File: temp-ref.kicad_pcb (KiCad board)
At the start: 4 copper layers, 172.5 x 76.5 mm, 42 parts, among them IC1 INA211AIDCKT, IC2 INA211AIDCKT, J1 Conn_01x05_Male, J2 USB_C_Receptacle_USB2.0, Q1 Q_NMOS_GDS, Q3 Q_NMOS_GDS, SW1 SW_SPST, SW2 SW_SPST, SW3 SW_SPST, SW4 SW_SPST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

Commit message: layout attempt 1
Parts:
- added Q2: MMBT3904, Package_TO_SOT_SMD:SOT-23, F.Cu at (151.8, 48.4)
- added R3: 10k, Resistor_SMD:R_0603_1608Metric, F.Cu at (151.6, 52.6)
- added R5: 10k, Resistor_SMD:R_0603_1608Metric, F.Cu at (151.6, 51.0)
- added R9: 33, Resistor_SMD:R_0603_1608Metric, F.Cu at (148.6, 47.4)
- J2: footprint Connector_USB:USB_C_Receptacle_JAE_DX07S024WJ3R400 -> Connector_USB:USB_C_Receptacle_Amphenol_12401610E4-2A
- SW1, SW2, SW3, SW4: footprint Button_Switch_SMD:SW_Push_1P1T_NO_CK_KSC7xxJ -> temp-ref:5.2mm_Tact_reverse_mount
- U6: value adafruit-tft-120x135-4383 -> spi-tft-1.14-240x135; footprint temp-ref:adafruit-tft-4383 -> temp-ref:TFT-1.14-240-135; moved to B.Cu
- moved U5 84.9 mm to (31.8, 61.6)
- moved U1 55.6 mm to (94.2, 60.0)
- moved U6 16.7 mm to (135.5, 32.7), turned to 90 degrees
- moved IC1 12.3 mm to (148.0, 85.3), turned to 270 degrees
- moved IC2 11.5 mm to (138.0, 85.3), turned to 270 degrees
- moved C8 10.8 mm to (148.1, 87.8), turned to 180 degrees
- moved J2 10.1 mm to (143.0, 95.5), turned to 0 degrees
- moved C5 9.80 mm to (137.9, 87.8), turned to 180 degrees
- moved U7 6.86 mm to (145.1, 86.0), turned to 180 degrees
- moved U10 6.22 mm to (140.9, 86.0), turned to 180 degrees
- turned SW1 to 90 degrees
- turned SW2 to 90 degrees
- turned SW3 to 90 degrees
- turned SW4 to 90 degrees
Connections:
- U4 pad 10: Net-(U4-Pad10) -> WIFI_G2
- U4 pad 15: Net-(U4-Pad15) -> WIFI_TX
- U4 pad 16: Net-(U4-Pad16) -> WIFI_RX
- U4 pad 21: Net-(U4-Pad21) -> WIFI_G0
- U4 pad 9: Net-(U4-Pad9) -> WIFI_RST
- U6 pad 1: +3V3 -> (no net)
- U6 pad 10: DISP_SDCS -> +3V3
- U6 pad 11: DISP_BACKLIGHT -> Net-(R9-Pad2)
- U6 pad 2: Net-(U6-Pad2) -> (no net)
- U6 pad 3: GND -> DISP_MOSI
- U6 pad 5: DISP_MISO -> DISP_DC
- U6 pad 6: DISP_MOSI -> DISP_RST
- U6 pad 8: DISP_RST -> GND
- U6 pad 9: DISP_DC -> (no net)
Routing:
- net SCL: track 13.4 -> 183.3 mm, vias 0 -> 5
- net +3V3: track 39.4 -> 183.7 mm, vias 13 -> 15
- net SDA: track 12.9 -> 148.0 mm, vias 0 -> 3
- net KEYB: track 1.24 -> 41.0 mm, vias 1 -> 0
- net VBUS: track 35.5 -> 72.0 mm, vias 14 -> 28
- net KEYA: track 1.04 -> 34.7 mm, vias 1 -> 0
- net DISP_SCK: track 0.00 -> 31.9 mm, vias 0 -> 3
- net DISP_MOSI: track 0.00 -> 31.6 mm, vias 0 -> 3
- net DISP_BACKLIGHT: track 0.00 -> 28.1 mm, vias 0 -> 2
- net KEYC: track 1.14 -> 26.9 mm, vias 1 -> 0
- net KEYD: track 1.12 -> 24.4 mm, vias 1 -> 0
- net B_SENSE: track 39.2 -> 16.0 mm, vias 4 -> 3
- net DISP_CS: track 0.00 -> 22.6 mm, vias 0 -> 1
- net DISP_RST: track 0.00 -> 22.6 mm, vias 0 -> 1
- net DISP_DC: track 0.00 -> 22.3 mm, vias 0 -> 1
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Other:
- outline, holes or cut-outs redrawn
- rule pad_to_mask_clearance: 0.002 -> 0

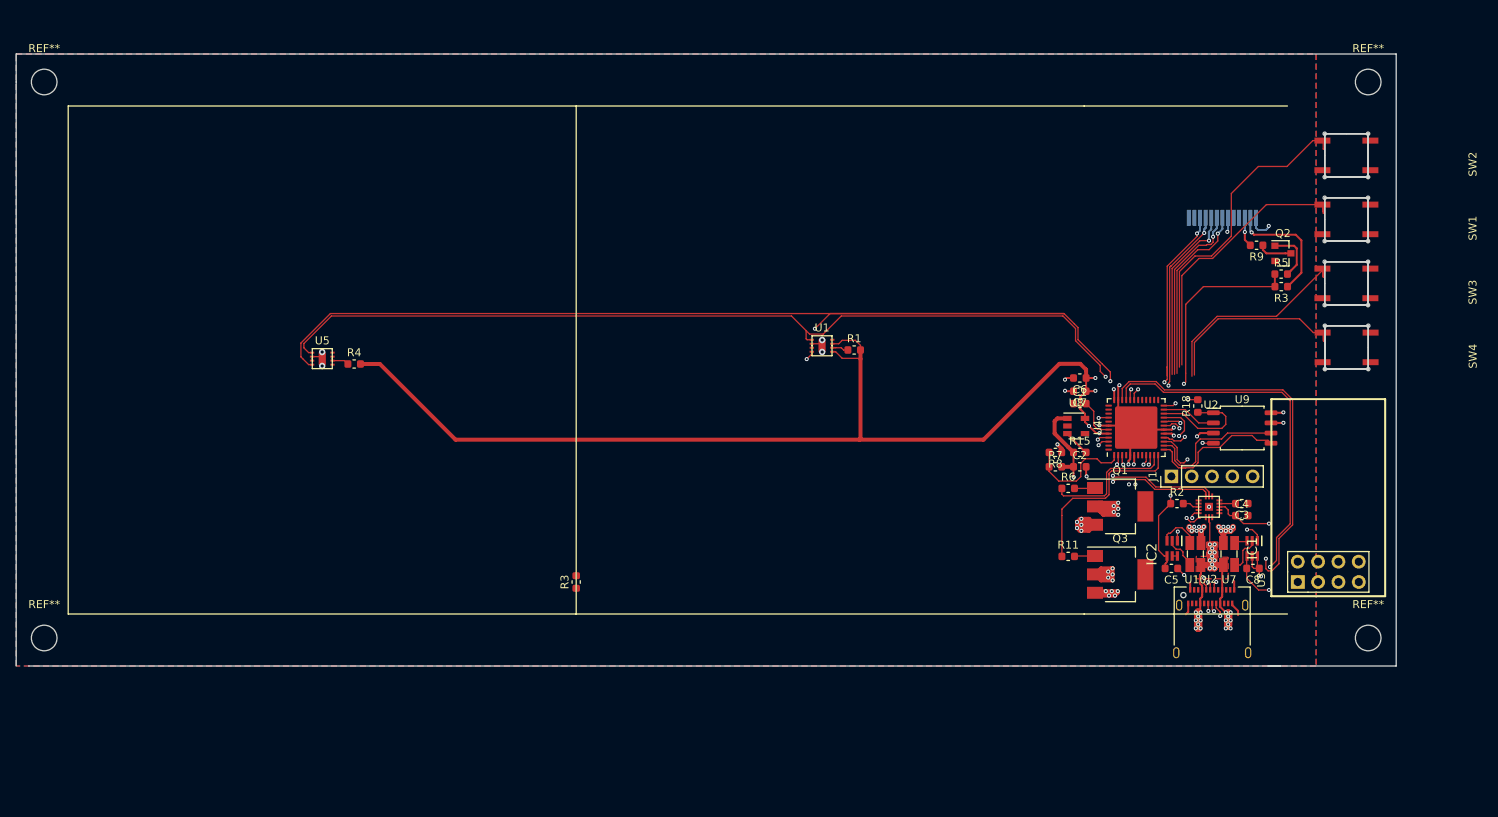
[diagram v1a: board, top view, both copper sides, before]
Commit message: REworked electronics into smaller board. Heating elements will be seperate.
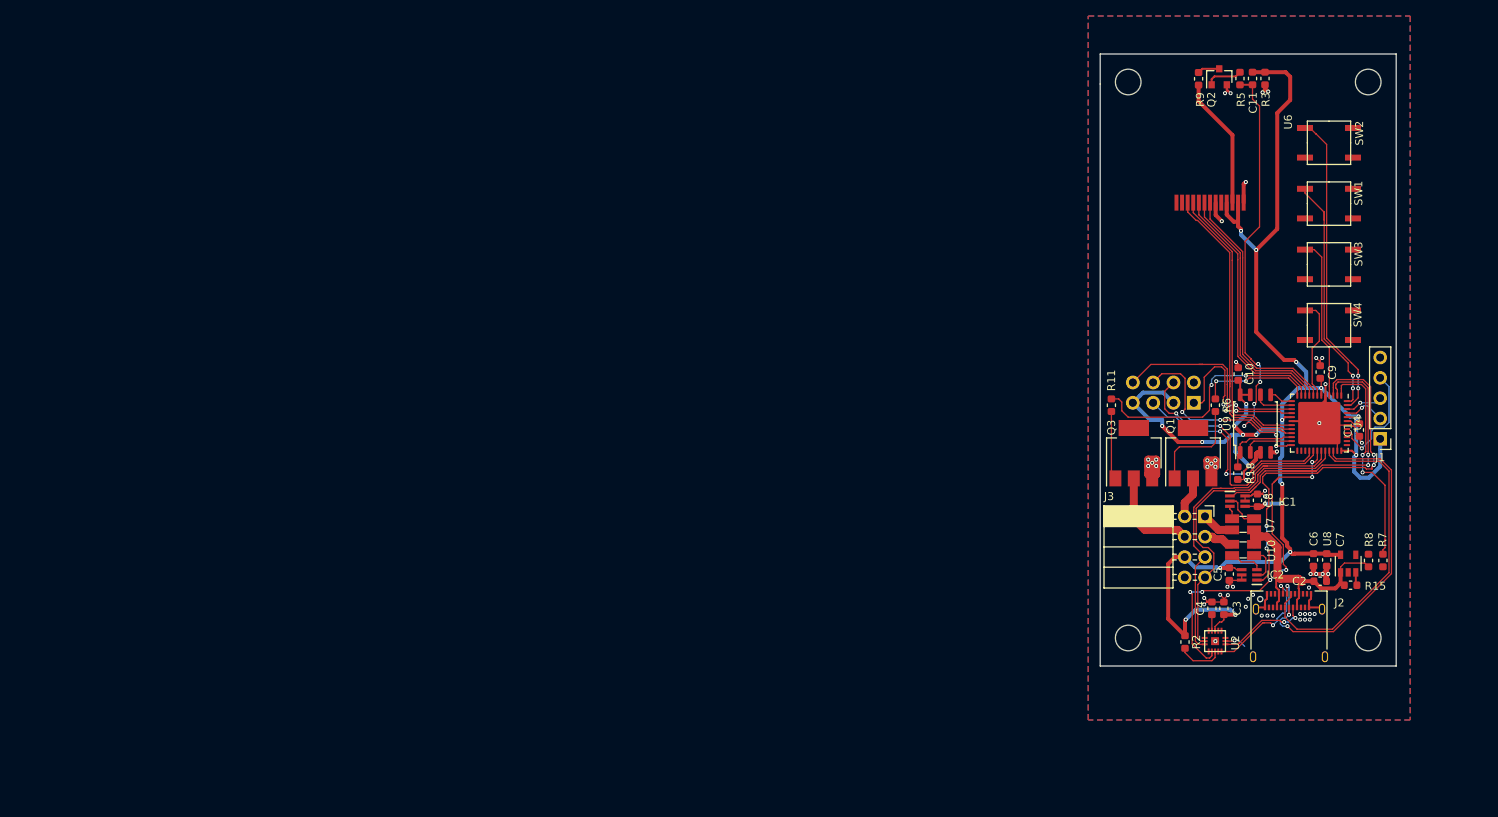
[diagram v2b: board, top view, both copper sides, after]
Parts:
- removed R1, R4: 1k, Resistor_SMD:R_0603_1608Metric
- removed the R3 at (63.5, 89.5)
- removed the REF** at (-3.00, 96.5)
- removed the REF** at (-3.00, 27.0)
- removed U1, U5: STS-30-DIS, temp-ref:sts
- added C10: 1uF, Capacitor_SMD:C_0603_1608Metric, F.Cu at (146.2, 63.5)
- added C11: 1uF, Capacitor_SMD:C_0603_1608Metric, F.Cu at (149.6, 26.6)
- added C9: 1uF, Capacitor_SMD:C_0603_1608Metric, F.Cu at (156.5, 63.2)
- added J3: Conn_02x04_Counter_Clockwise, Connector_PinSocket_2.54mm:PinSocket_2x04_P2.54mm_Horizontal, F.Cu at (142.1, 81.3)
- added REF**: MountingHole_3.2mm_M3, MountingHole:MountingHole_3.2mm_M3, F.Cu at (132.5, 96.5)
- added REF**: MountingHole_3.2mm_M3, MountingHole:MountingHole_3.2mm_M3, F.Cu at (132.5, 27.0)
- U3: moved to B.Cu
- U6: moved to F.Cu
- moved R8 43.1 mm to (164.3, 86.8), turned to 90 degrees
- moved R7 40.9 mm to (162.5, 86.8), turned to 270 degrees
- moved U8 38.1 mm to (160.0, 87.2), turned to 90 degrees
- moved R15 37.7 mm to (160.3, 89.9)
- moved C7 37.4 mm to (157.3, 86.7), turned to 270 degrees
- moved C6 37.0 mm to (155.7, 86.7), turned to 270 degrees
- moved C1 35.1 mm to (161.4, 70.5), turned to 90 degrees
- moved C2 33.3 mm to (156.5, 89.4)
- moved J1 26.5 mm to (164.0, 71.6), turned to 180 degrees
- moved R3 26.3 mm to (148.0, 26.6), turned to 270 degrees
- moved U3 25.9 mm to (140.7, 67.1)
- moved R5 25.0 mm to (146.5, 26.6), turned to 90 degrees
- moved Q2 23.5 mm to (143.9, 26.4), turned to 90 degrees
- moved U4 22.9 mm to (156.4, 69.6), turned to 270 degrees
- moved R9 22.0 mm to (141.3, 26.6), turned to 270 degrees
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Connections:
- Q1 pad 2: ZONEA -> ZONEA-
- Q3 pad 2: ZONEB -> ZONEB-
- U10 pad 3: ZONEB -> ZONEB+
- U4 pad 10: WIFI_G2 -> DISP_DC
- U4 pad 11: HEATER0 -> HEATER1
- U4 pad 12: HEATER1 -> HEATER0
- U4 pad 2: B_SENSE -> A_SENSE
- U4 pad 28: Net-(U4-Pad28) -> WIFI_RST
- U4 pad 29: Net-(U4-Pad29) -> WIFI_G2
- U4 pad 3: A_SENSE -> B_SENSE
- U4 pad 30: Net-(U4-Pad30) -> PD_ALERT
- U4 pad 4: Net-(U4-Pad4) -> KEYC
- U4 pad 47: Net-(U4-Pad47) -> KEYB
- U4 pad 48: Net-(U4-Pad48) -> KEYA
- U4 pad 7: Net-(U4-Pad7) -> KEYD
- U4 pad 8: Net-(U4-Pad8) -> DISP_CS
- U4 pad 9: WIFI_RST -> DISP_RST
- U7 pad 4: ZONEA -> ZONEA+
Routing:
- net ZONEB: track 4060.3 -> 0.00 mm, vias 12 -> 0
- net ZONEA: track 3705.1 -> 0.00 mm, vias 12 -> 0
- net SCL: track 183.3 -> 39.6 mm, vias 5 -> 0
- net SDA: track 148.0 -> 39.7 mm, vias 3 -> 0
- net PD_ALERT: track 0.00 -> 44.9 mm, vias 0 -> 6
- net VBUS: track 72.0 -> 36.3 mm, vias 28 -> 1
- net +3V3: track 183.7 -> 214.9 mm, vias 15 -> 22
- net B_SENSE: track 16.0 -> 46.1 mm, vias 3 -> 4
- net DISP_BACKLIGHT: track 28.1 -> 55.3 mm, vias 2 -> 6
- net GND: track 72.4 -> 93.6 mm, vias 28 -> 48
- net A_SENSE: track 25.7 -> 44.9 mm, vias 3 -> 2
- net D+: track 64.5 -> 46.3 mm
- net D-: track 58.1 -> 41.3 mm, vias 3 -> 0
- net WIFI_TX: track 36.6 -> 20.5 mm, vias 1 -> 2
- net FLMOSI: track 18.6 -> 2.96 mm
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- removed copper zone on In2.Cu, net +3V3
- removed copper zone on In1.Cu, net GND
- removed copper zone on F.Cu, net VBUS
- removed copper zone on In2.Cu, net VBUS
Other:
- board size 172.5 x 76.5 mm -> 37 x 76.5 mm
- copper layers 4 -> 2

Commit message: Update temp-ref.kicad_pcb
removed errant via
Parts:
- added D1: SK6812, LED_SMD:LED_SK6812_PLCC4_5.0x5.0mm_P3.2mm, F.Cu at (157.6, 80.2)
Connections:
- U4 pad 27: Net-(U4-Pad27) -> neopix
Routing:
- net neopix: track 0.00 -> 13.8 mm, vias 0 -> 2
- net VBUS: track 36.3 -> 45.2 mm
- net +3V3: track 214.9 -> 218.7 mm
- net GND: track 93.6 -> 96.4 mm, vias 48 -> 49
- net (no net): vias 2 -> 1

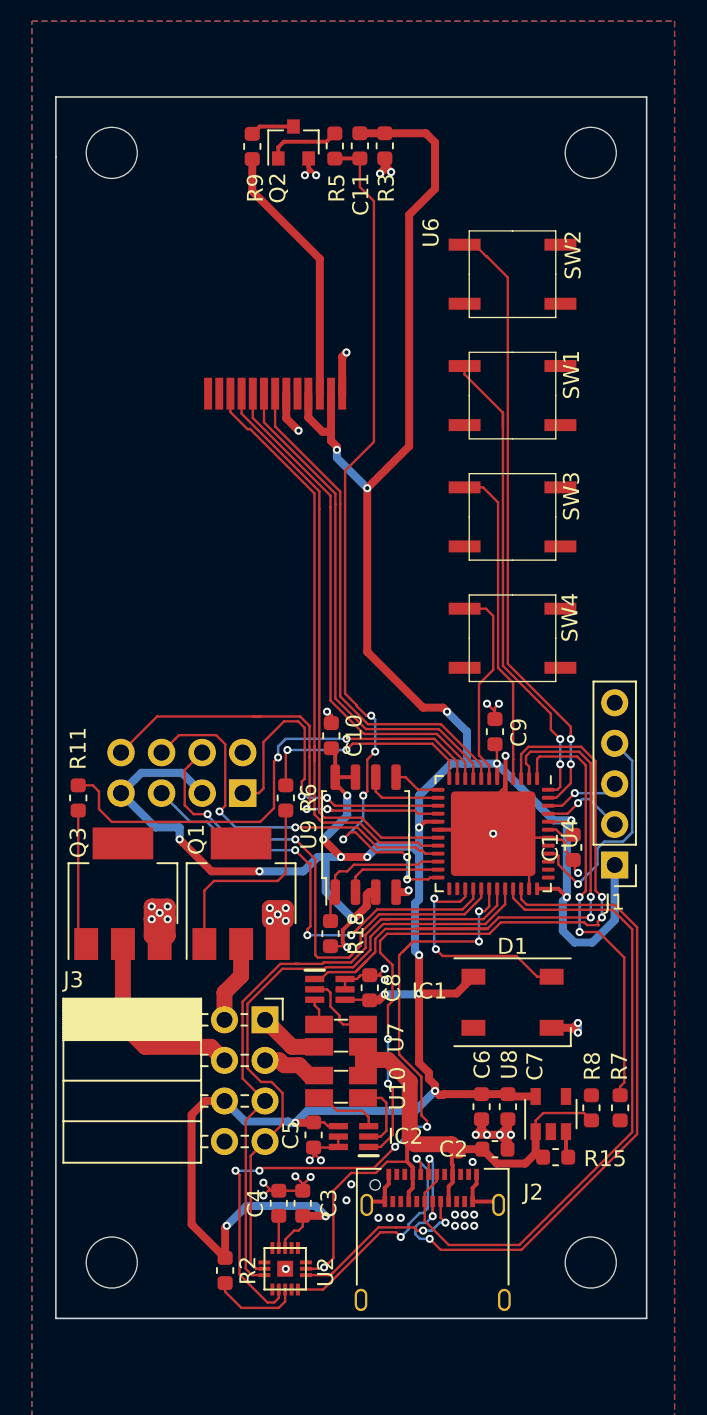
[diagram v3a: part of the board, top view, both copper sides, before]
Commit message: 3d models added, Added dallas pins, added nepixels, moved some elements around.
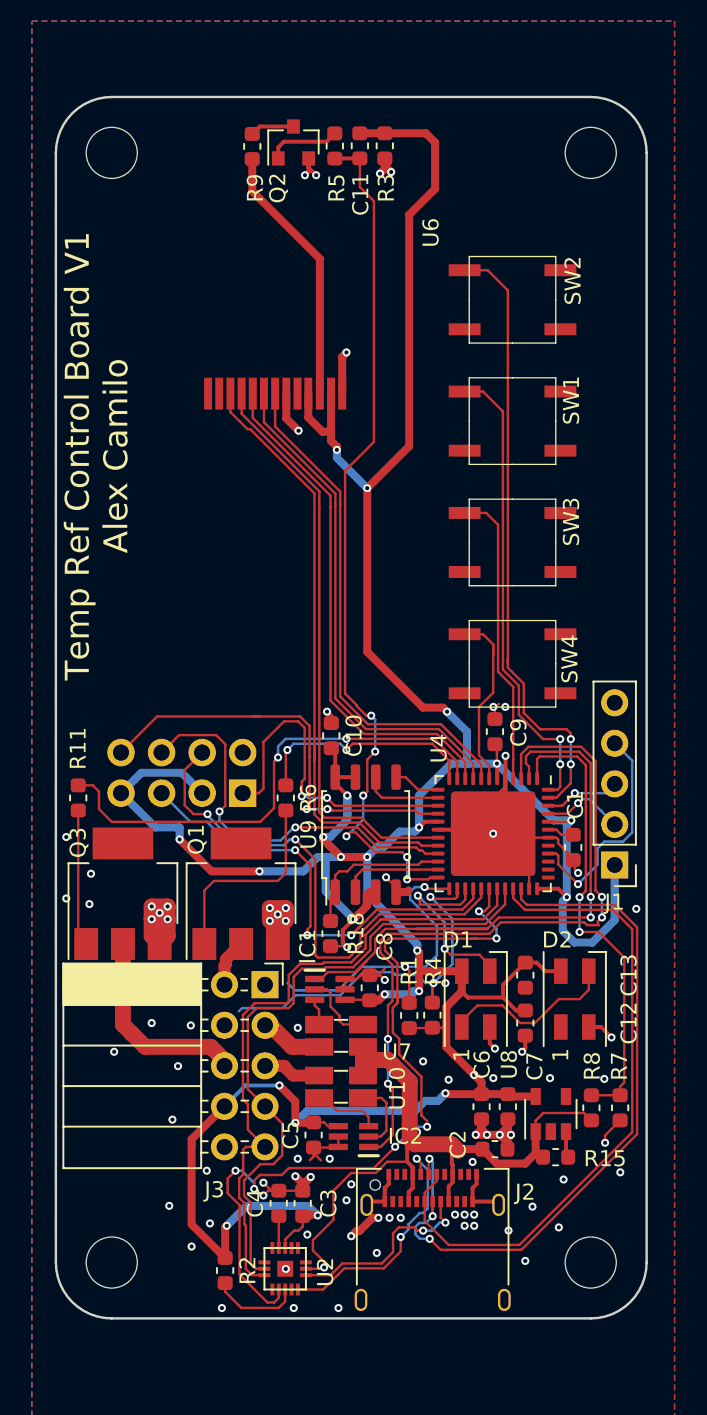
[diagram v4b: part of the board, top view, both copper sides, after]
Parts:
- added C12: 1uF, Capacitor_SMD:C_0603_1608Metric, F.Cu at (158.4, 81.5)
- added C13: 1uF, Capacitor_SMD:C_0603_1608Metric, F.Cu at (158.4, 78.5)
- added D2: SK6812MINI, temp-ref:LED_SK6812MINI_PLCC4_3.5x3.5mm_P1.75mm, F.Cu at (161.5, 80.0)
- added R1: 4.7k, Resistor_SMD:R_0603_1608Metric, F.Cu at (151.1, 81.0)
- added R4: 4.7k, Resistor_SMD:R_0603_1608Metric, F.Cu at (152.6, 81.0)
- D1: value SK6812 -> SK6812MINI; footprint LED_SMD:LED_SK6812_PLCC4_5.0x5.0mm_P3.2mm -> temp-ref:LED_SK6812MINI_PLCC4_3.5x3.5mm_P1.75mm
- J2: footprint Connector_USB:USB_C_Receptacle_Amphenol_12401610E4-2A -> temp-ref:USB_C_Receptacle_Amphenol_12401610E4-2A
- J3: value Conn_02x04_Counter_Clockwise -> Conn_02x05_Odd_Even; footprint Connector_PinSocket_2.54mm:PinSocket_2x04_P2.54mm_Horizontal -> Connector_PinSocket_2.54mm:PinSocket_2x05_P2.54mm_Horizontal
- U9: footprint Package_SO:SOIC-8_5.23x5.23mm_P1.27mm -> temp-ref:SOIC-8_5.23x5.23mm_P1.27mm
- moved D1 2.31 mm to (155.3, 80.0), turned to 90 degrees
- moved J3 2.20 mm to (142.1, 79.1)
- moved SW2 1.60 mm to (157.6, 36.2)
- moved SW3 1.60 mm to (157.6, 51.4)
- moved SW4 1.60 mm to (157.6, 59.0)
- moved SW1 1.60 mm to (157.6, 43.8)
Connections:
- D1 pad 1: GND -> Net-(D1-Pad1)
- D1 pad 2: neopix -> GND
- D1 pad 3: +3V3 -> neopix
- D1 pad 4: Net-(D1-Pad4) -> +3V3
- J3 pad 1: ZONEA+ -> DALLAS1
- J3 pad 3: ZONEB+ -> ZONEA+
- J3 pad 4: ZONEB- -> DALLAS2
- J3 pad 5: SDA -> ZONEB+
- J3 pad 6: +3V3 -> ZONEB-
- J3 pad 8: GND -> +3V3
- U4 pad 25: Net-(U4-Pad25) -> DALLAS1
- U4 pad 26: Net-(U4-Pad26) -> DALLAS2
- U4 pad 49: (no net) -> GND
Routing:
- net DALLAS2: track 0.00 -> 24.8 mm, vias 0 -> 2
- net DALLAS1: track 0.00 -> 20.3 mm, vias 0 -> 2
- net +3V3: track 218.7 -> 235.5 mm, vias 22 -> 24
- net Net-(D1-Pad1): track 0.00 -> 11.2 mm
- net GND: track 96.4 -> 102.7 mm, vias 49 -> 83
- net PD_ALERT: track 44.9 -> 50.7 mm
- net ZONEA-: track 5.18 -> 2.98 mm
- net VBUS_SENSE: track 27.4 -> 29.2 mm
- net neopix: track 13.8 -> 12.3 mm
- net KEYC: track 20.2 -> 18.7 mm
- net SCL: track 39.6 -> 40.9 mm
- net SDA: track 39.7 -> 41.0 mm
- net KEYA: track 30.6 -> 29.5 mm
- net VBUS: track 45.2 -> 46.3 mm
- net KEYD: track 12.8 -> 11.7 mm
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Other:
- outline, holes or cut-outs redrawn
- board text added: "Temp Ref Control Board V1 Alex Camilo"
- board text added: "github.com/acamilo/Cheap-Feaver-Screener-PID-Control-PCB"
